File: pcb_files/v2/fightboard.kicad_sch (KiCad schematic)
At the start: 32 parts, among them J1 SW_Push, K1 SW_Push, M1 XIAO-RP2040, P1 SW_Push, U1 SW_Push, U2 MCP23018-E_SS

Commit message: add v2 pcb
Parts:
- removed U2: MCP23018-E_SS, kb_lib:SOIC127P600X175-14N, symbol dk_Interface-I-O-Expanders:MCP23018-E_SP
- added C104: C_Small, Resistor_SMD:R_2010_5025Metric_Pad1.40x2.65mm_HandSolder, symbol Device:C_Small
- added IOEX2: MCP23018-E_SS, SOP65P780X200-24N, symbol MCP23018-SS:MCP23018-E_SS
- added R330: R_US, Resistor_SMD:R_2010_5025Metric_Pad1.40x2.65mm_HandSolder, symbol Device:R_US
- ;1, A1, D1, I1, J1, K1, L1, O1, P1, S1, U1, W1: footprint keyswitches:Kailh_socket_MX -> kb_lib:mx-choc socket keyswitch
- LED0: renamed from LED1; footprint keyswitches:Kailh_socket_MX -> Button_Switch_THT:SW_PUSH_6mm
- gave numbers to parts that had none: 13
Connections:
- net at ;1.1, A1.1, BKSP1.1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: now also C104.2, IOEX2.1 (VSS), IOEX2.13 (ADDR)
- net at MNUS1.2: now also IOEX2.2 (GPB0)
- net at LD1.14 (VCC), LED1.1 (VDD), LED10.1 (VDD)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: now also C104.1
- net at LD1.3 (1Y): now also R330.2; no longer LED1.4 (DIN)
- net at L1.2: now also IOEX2.19 (GPA2)
- net at ;1.2: now also IOEX2.20 (GPA3)
- net at U1.2: now also IOEX2.6 (GPB4)
- net at W1.2: now also IOEX2.24 (GPA7)
- net at A1.2: now also IOEX2.23 (GPA6)
- net at P1.2: now also IOEX2.9 (GPB7)
- net at I1.2: now also IOEX2.7 (GPB5)
- net at K1.2: now also IOEX2.18 (GPA1)
- net at PLUS1.2: now also IOEX2.3 (GPB1)
- net at O1.2: now also IOEX2.8 (GPB6)
- net at ESC1.2: now also IOEX2.5 (GPB3)
- net at M1.12 (3V3): now also IOEX2.10 (VDD)
- net at M1.6 (D5): now also IOEX2.11 (SCL)
- net at M1.5 (D4): now also IOEX2.12 (SDA)
- net at M1.2 (D1): now also IOEX2.14 (~{RESET})
- net at D1.2: now also IOEX2.21 (GPA4)
- net at S1.2: now also IOEX2.22 (GPA5)
- net at J1.2: now also IOEX2.17 (GPA0)
- net at BKSP1.2: now also IOEX2.4 (GPB2)
- new net: LED1.4 (DIN), R330.1
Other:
- moved on the sheet: ;1, A1, BKSP1, D1, ESC1, I1, J1, K1, L1, MNUS1, O1, P1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

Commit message: update v2 pcb
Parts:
- removed C104: C_Small, Resistor_SMD:R_2010_5025Metric_Pad1.40x2.65mm_HandSolder, symbol Device:C_Small
- removed LD1: SN74AHCT125D, SOIC127P600X175-14N, symbol SN74HCT125D:SN74AHCT125D
- added C1, C10, C11, C12, C13, C2, C3, C4, C5, C6, C7, C8, C9: C_Small, Resistor_SMD:R_2010_5025Metric_Pad1.40x2.65mm_HandSolder, symbol Device:C_Small
- added LED13: WS2812B, kb_lib:Reverse Mount SK6812MINI-E, symbol LED:WS2812B
- added LS1: TXB0108PWR, SOP65P640X120-20N, symbol TXB0108PWR:TXB0108PWR
- renumbered ESC1 to ENTR1, IOEX2 to IOEX1
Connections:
- net at ;1.1, A1.1, BKSP1.1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: now also C1.2, C10.2, C11.2, C12.2, C13.2, C2.2, C3.2, C4.2, C5.2, C6.2, C7.2, C8.2, C9.2, LED13.3 (VSS), LS1.11 (GND)
- net at LED1.1 (VDD), LED10.1 (VDD), LED11.1 (VDD)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: now also C1.1, C10.1, C11.1, C12.1, C13.1, C2.1, C3.1, C4.1, C5.1, C6.1, C7.1, C8.1, C9.1, LED13.1 (VDD), LS1.19 (VCCB)
- net at M1.1 (D0): now also LS1.1 (A1)
- net at R330.2: now also LS1.20 (B1)
- net at IOEX1.10 (VDD), M1.12 (3V3): now also LS1.2 (VCCA)
- net at IOEX1.14 (~{RESET}), M1.2 (D1): now also LS1.10 (OE)
- net at LED12.2 (DOUT): now also LED13.4 (DIN)
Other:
- moved on the sheet: ;1, A1, BKSP1, D1, ENTR1, I1, J1, K1, L1, LED0, LED1, LED10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

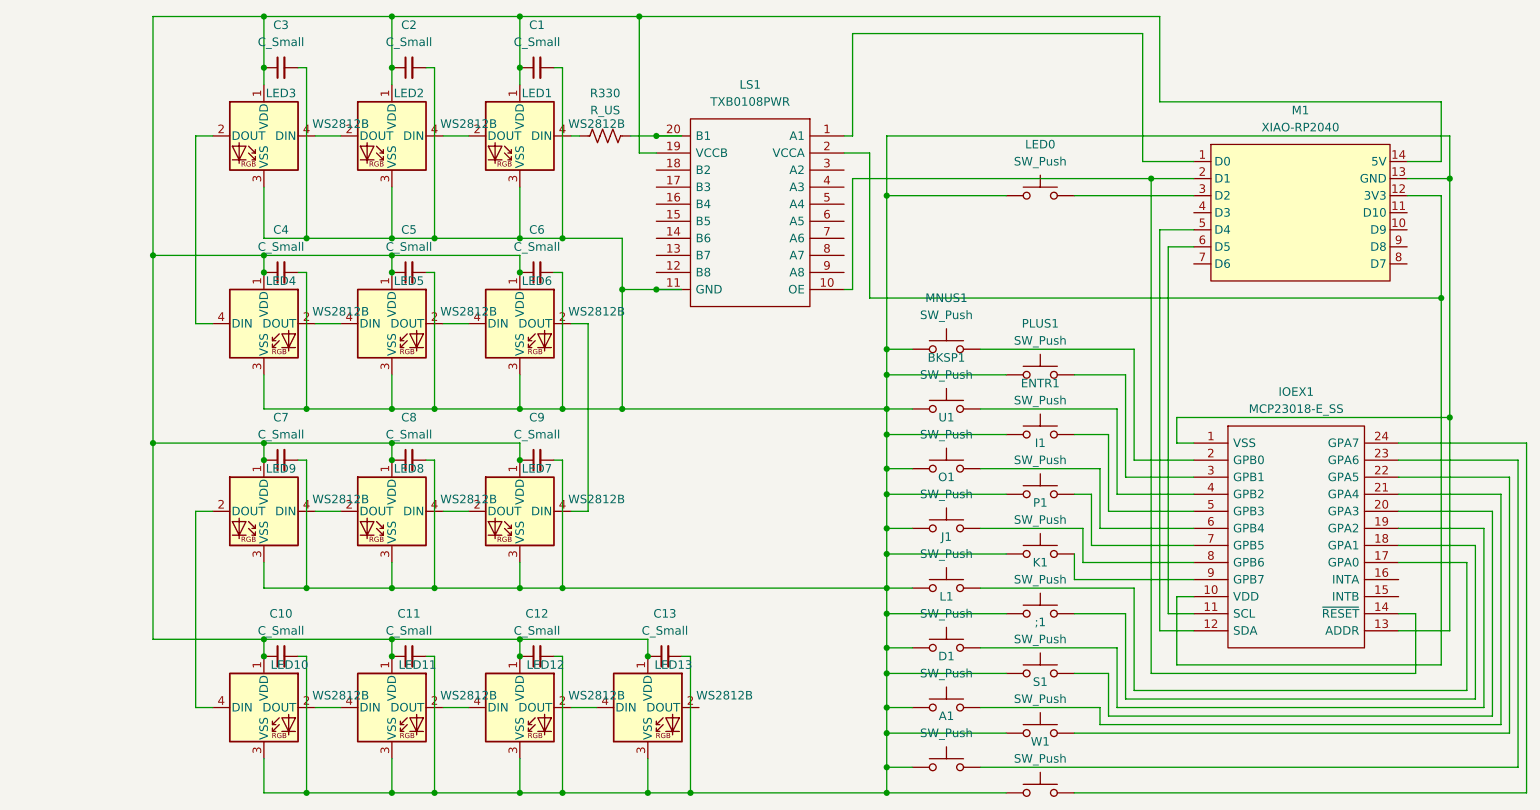
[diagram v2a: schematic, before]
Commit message: remove capacitors
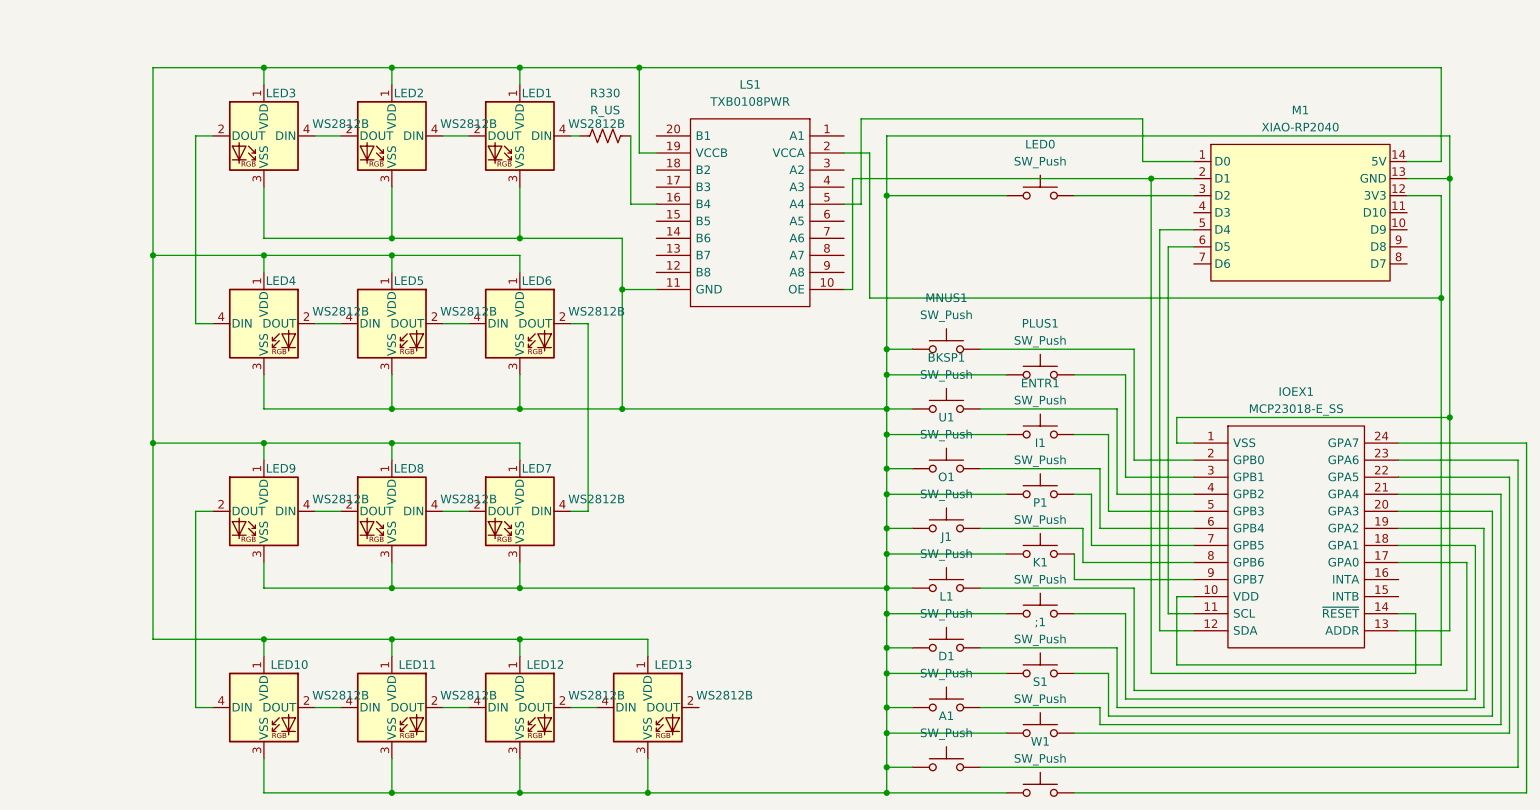
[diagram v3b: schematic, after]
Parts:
- removed C1, C10, C11, C12, C13, C2, C3, C4, C5, C6, C7, C8, C9: C_Small, Resistor_SMD:R_2010_5025Metric_Pad1.40x2.65mm_HandSolder, symbol Device:C_Small
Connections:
- net at LS1.1 (A1): no longer M1.1 (D0)
- net at LS1.16 (B4): now also R330.2
- net at LS1.20 (B1): no longer R330.2
- net at LS1.5 (A4): now also M1.1 (D0)
